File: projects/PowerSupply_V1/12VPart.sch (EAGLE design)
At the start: 10 parts, among them IC1 LM2596T, X1 IN, X2 OUT

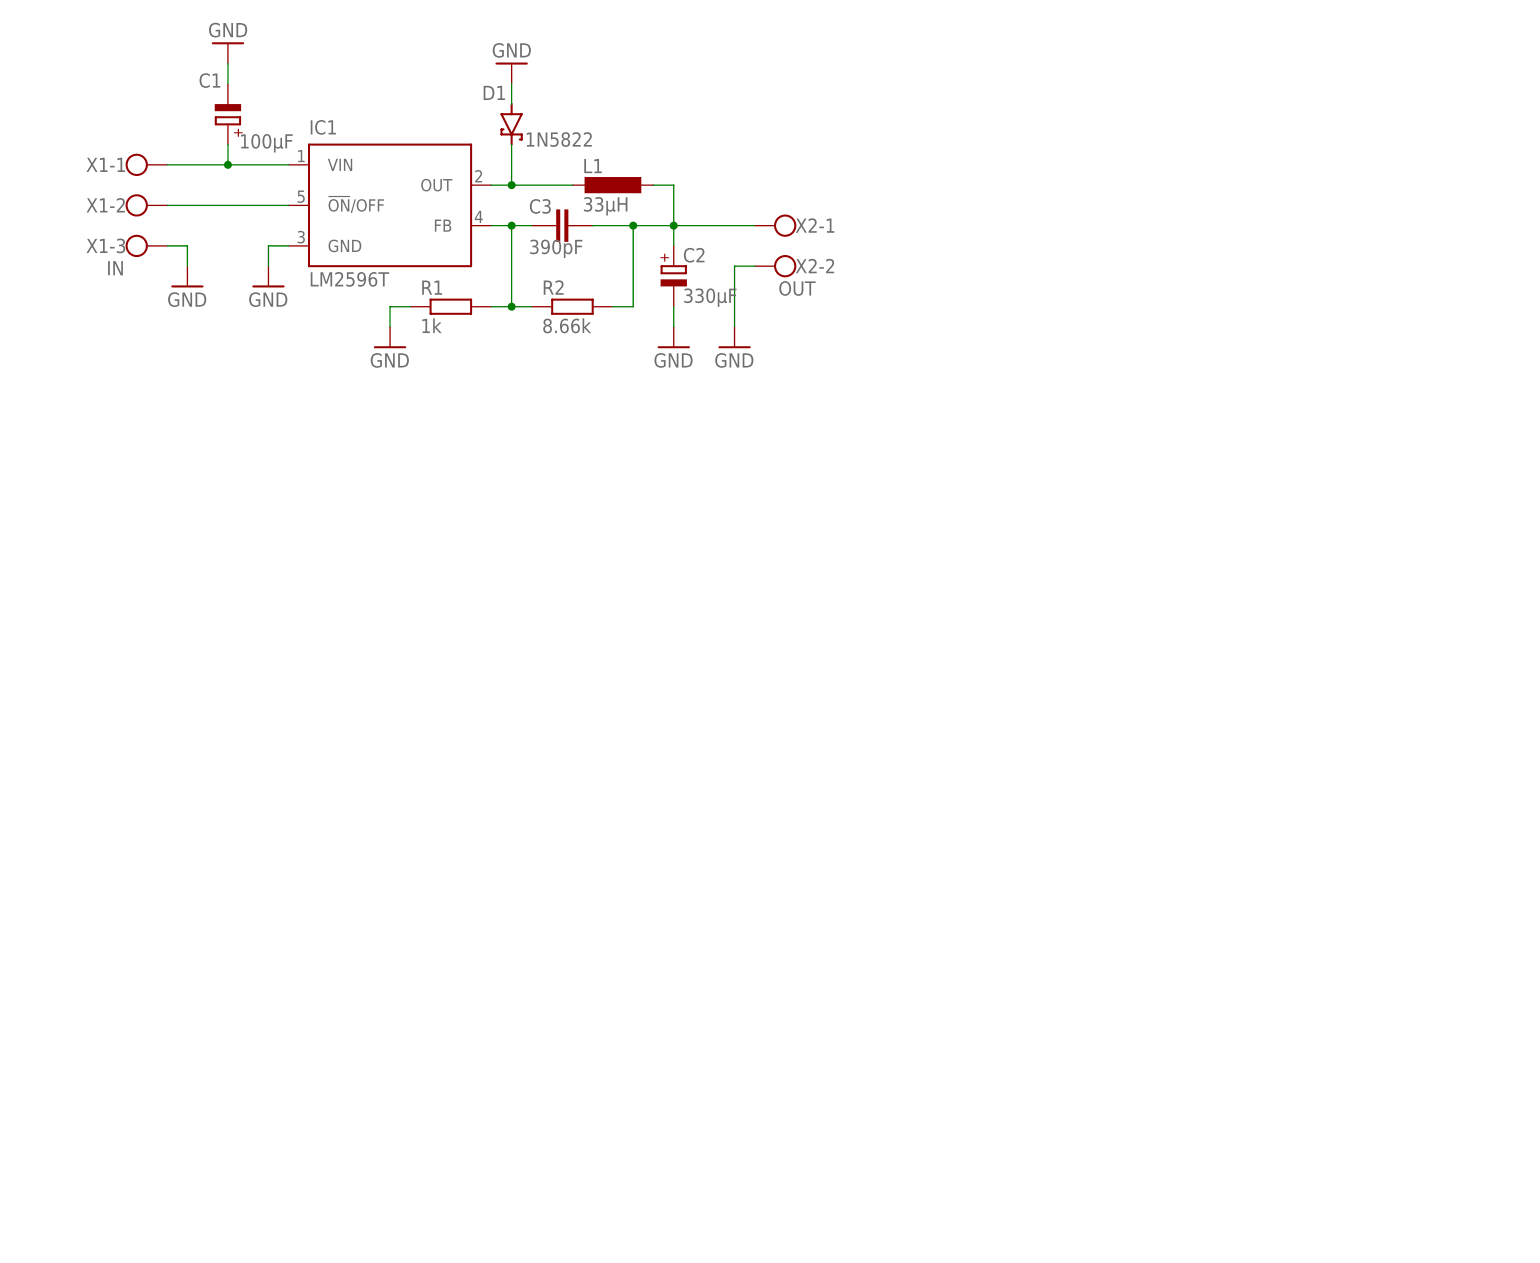
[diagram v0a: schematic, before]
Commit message: feat: power supply
changes:
- version one done
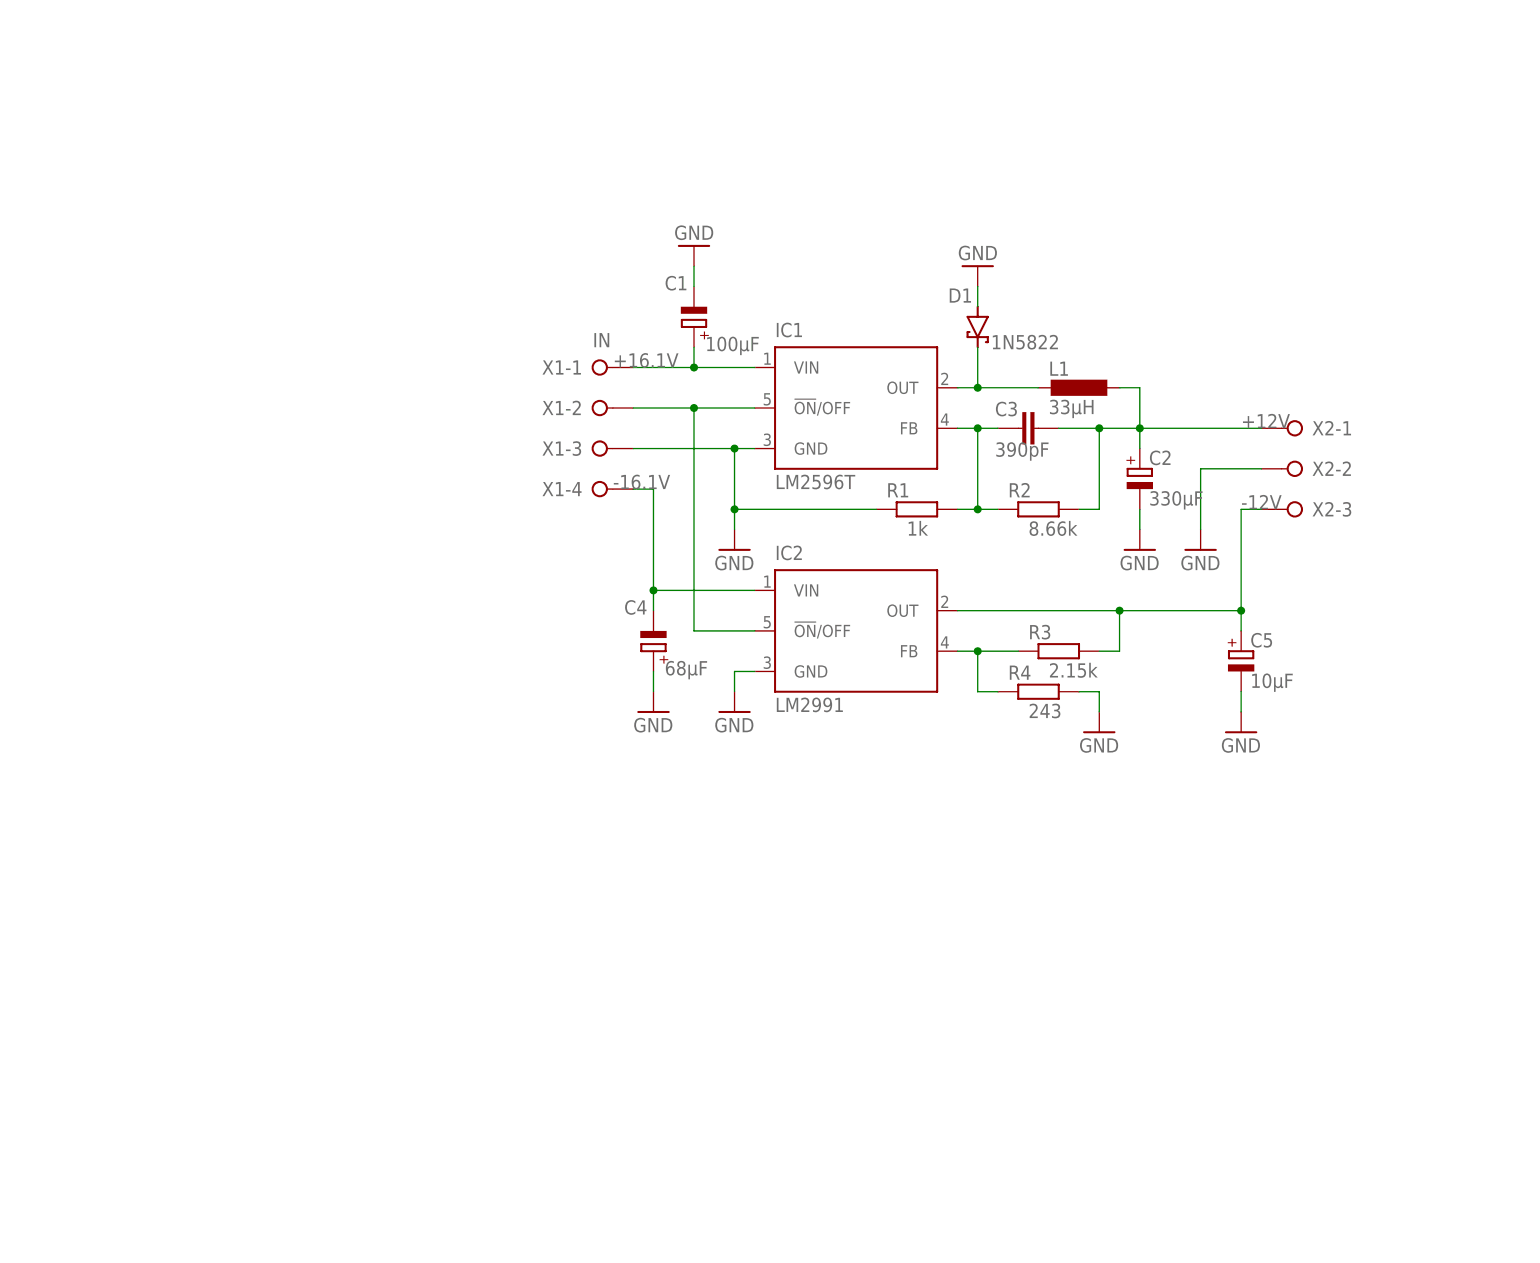
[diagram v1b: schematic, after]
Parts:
- added C4: 68µF, rcl:CPOL-EUE2.5-6
- added C5: 10µF, rcl:CPOL-EUE2.5-6
- added IC2: LM2991, national-semiconductor:LM2596T
- added R3: 2.15k, rcl:R-EU_0207/10
- added R4: 243, rcl:R-EU_0207/10
- C2: device rcl:CPOL-EUE3.5-8 -> rcl:CPOL-EUE2.5-6
- X1: device con-wago-500:W237-103 -> con-wago-508:W237-04P
- X2: value OUT -> (none); device con-wago-500:W237-102 -> con-wago-508:W237-03P
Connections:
- net N$3 renamed +12V
- net N$5 renamed +16.1V
- new net -12V: C5.+, IC2.OUT, R3.2, X2-3.KL
- new net -16.1V: C4.-, IC2.VIN, X1-4.KL
- new net N$3: IC2.FB, R3.1, R4.1
- net GND: now also C4.+, C5.-, IC2.GND, R4.2
- net N$2: now also IC2.!ON!/OFF
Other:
- moved on the sheet: C1, C2, C3, D1, IC1, L1, R1, R2

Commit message: feat: 12V part refactored
changes:
- schematic changed
- layout changed
- gerber files addeda
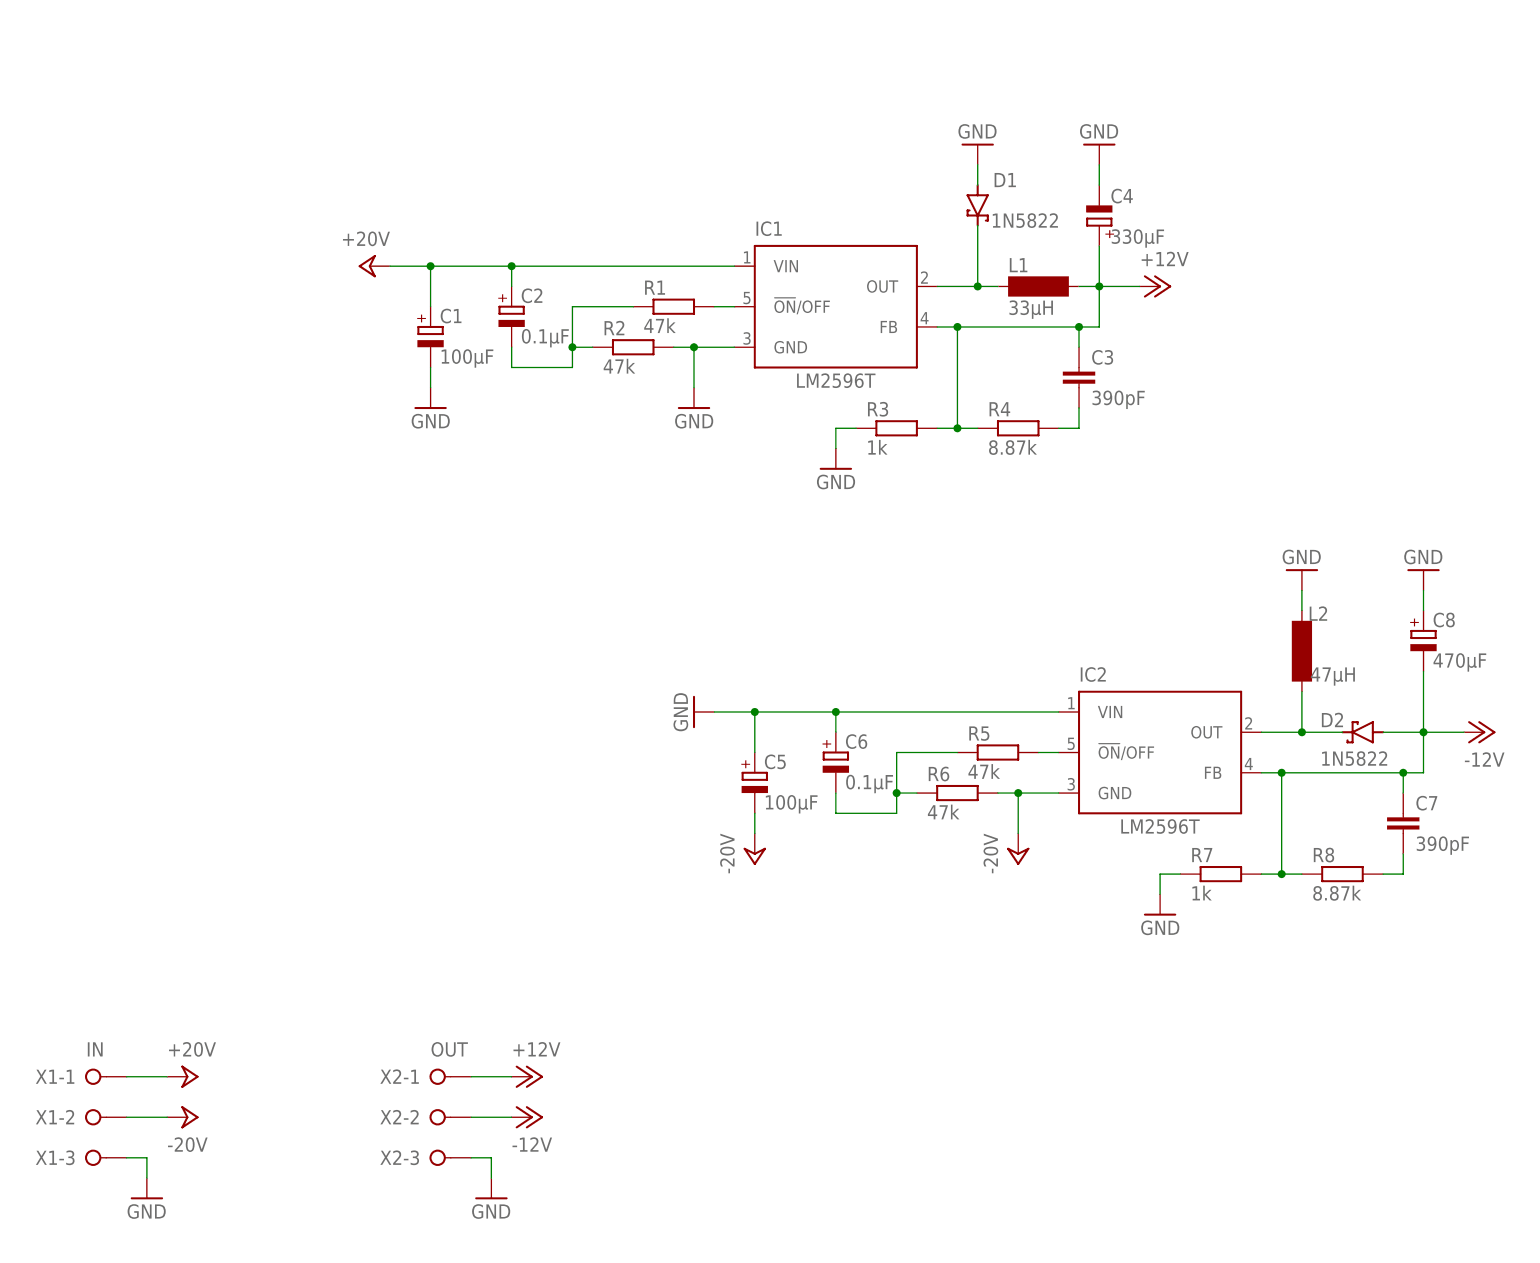
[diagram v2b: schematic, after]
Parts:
- added C6: 0.1µF, rcl:CPOL-EUE1.8-4
- added C7: 390pF, rcl:C-EU050-024X044
- added C8: 470µF, rcl:CPOL-EUE3.5-8
- added D2: 1N5822, diode:SCHOTTKY-DIODEC4111-15
- added L2: 47µH, inductor-neosid:SD12-680
- added R5, R6: 47k, rcl:R-EU_0207/10
- added R7: 1k, rcl:R-EU_0207/10
- added R8: 8.87k, rcl:R-EU_0207/10
- C2: value 330µF -> 0.1µF; device rcl:CPOL-EUE2.5-6 -> rcl:CPOL-EUE1.8-4
- C4: value 68µF -> 330µF; device rcl:CPOL-EUE2.5-6 -> rcl:CPOL-EUE3.5-8
- C5: value 10µF -> 100µF
- IC2: value LM2991 -> LM2596T
- L1: device rcl:L-EUTJ3-U2 -> inductor-neosid:SD12-680
- R1: value 1k -> 47k
- R2: value 8.66k -> 47k
- R3: value 2.15k -> 1k
- R4: value 243 -> 8.87k
- X1: device con-wago-508:W237-04P -> con-wago-508:W237-03P
- X2: value (none) -> OUT
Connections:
- removed net +16.1V: C1.+, IC1.VIN, X1-1.KL
- removed net -16.1V: C4.-, IC2.VIN, X1-4.KL
- new net +24V: C1.+, C2.+, IC1.VIN, X1-1.KL
- new net -24V: C5.-, IC2.GND, R6.2, X1-2.KL
- new net N$5: C7.2, R8.2
- new net N$6: C2.-, R1.1, R2.1
- new net N$7: IC2.!ON!/OFF, R5.2
- new net N$8: C6.-, R5.1, R6.1
- net +12V: now also C3.1, C4.+, IC1.FB, L1.2, R3.2, R4.1; no longer C2.+, C3.2, L1.1, R2.2
- net -12V: now also C7.1, C8.-, D2.A, IC2.FB, R7.2, R8.1, X2-2.KL; no longer C5.+, IC2.OUT, R3.2, X2-3.KL
- net GND: now also C4.-, C5.+, C6.+, C8.+, IC2.VIN, L2.2, R2.2, R3.1, R7.1, X2-3.KL; no longer C2.-, C4.+, C5.-, IC2.GND, R1.1, R4.2, X2-2.KL
- net N$1: now also C3.2, R4.2; no longer C3.1, IC1.FB, R1.2, R2.1
- net N$2: now also D2.C, IC2.OUT, L2.1; no longer IC1.!ON!/OFF, IC2.!ON!/OFF, X1-2.KL
- net N$3: now also D1.C, IC1.OUT, L1.1; no longer IC2.FB, R3.1, R4.1
- net N$4: now also IC1.!ON!/OFF, R1.2; no longer D1.C, IC1.OUT, L1.2
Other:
- moved on the sheet: C1, C2, C3, C4, C5, D1, IC1, IC2, L1, R1, R2, R3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

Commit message: refactor(12v): schematics changed
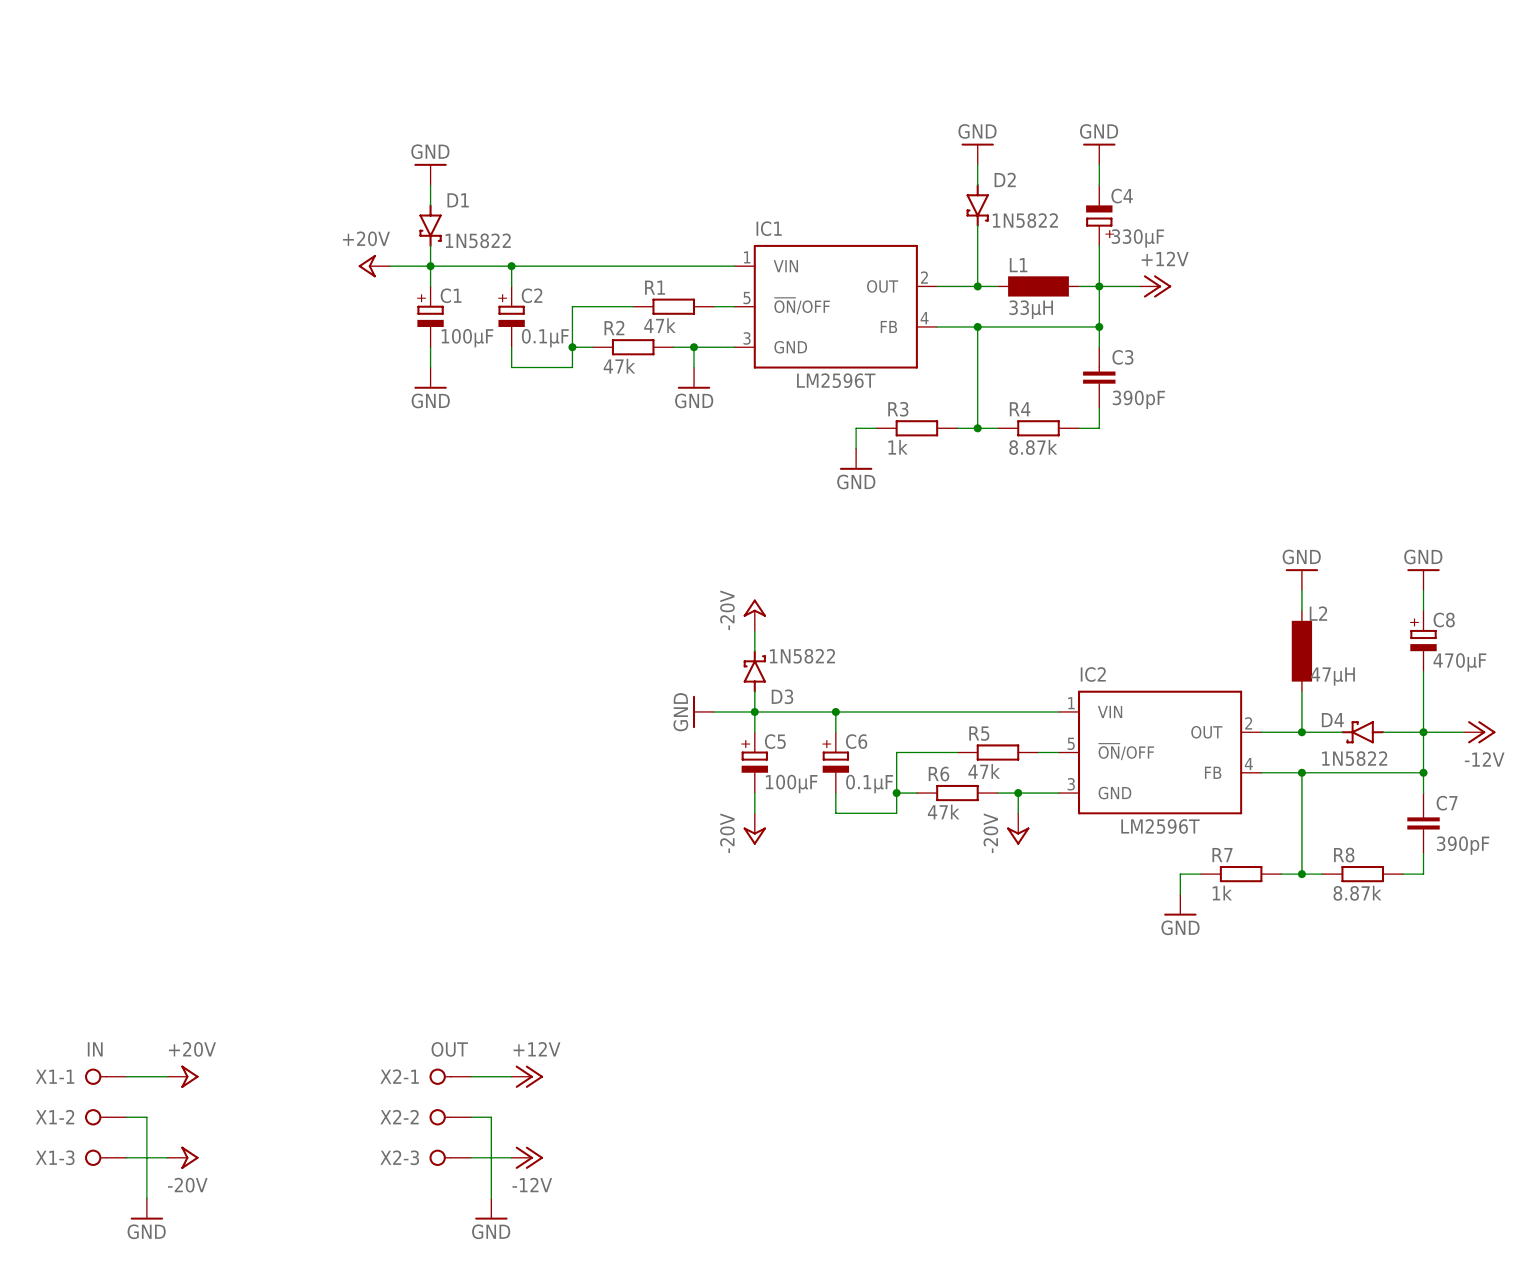
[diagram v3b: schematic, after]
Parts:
- added D3, D4: 1N5822, diode:SCHOTTKY-DIODEC4111-15
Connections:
- net +24V: now also D1.C
- net -12V: now also D4.A, X2-3.KL; no longer D2.A, X2-2.KL
- net -24V: now also D3.C, X1-3.KL; no longer X1-2.KL
- net GND: now also D2.A, D3.A, X1-2.KL, X2-2.KL; no longer X1-3.KL, X2-3.KL
- net N$2: now also D4.C; no longer D2.C
- net N$3: now also D2.C; no longer D1.C
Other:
- moved on the sheet: C1, C3, C5, C7, D1, D2, R3, R4, R7, R8
